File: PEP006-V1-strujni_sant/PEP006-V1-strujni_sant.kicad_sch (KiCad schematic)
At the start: 15 parts, among them J1 Screw_Terminal_01x02, J2 Conn_01x02_Pin, J3 Conn_01x02_Pin, J4 Conn_01x02_Pin

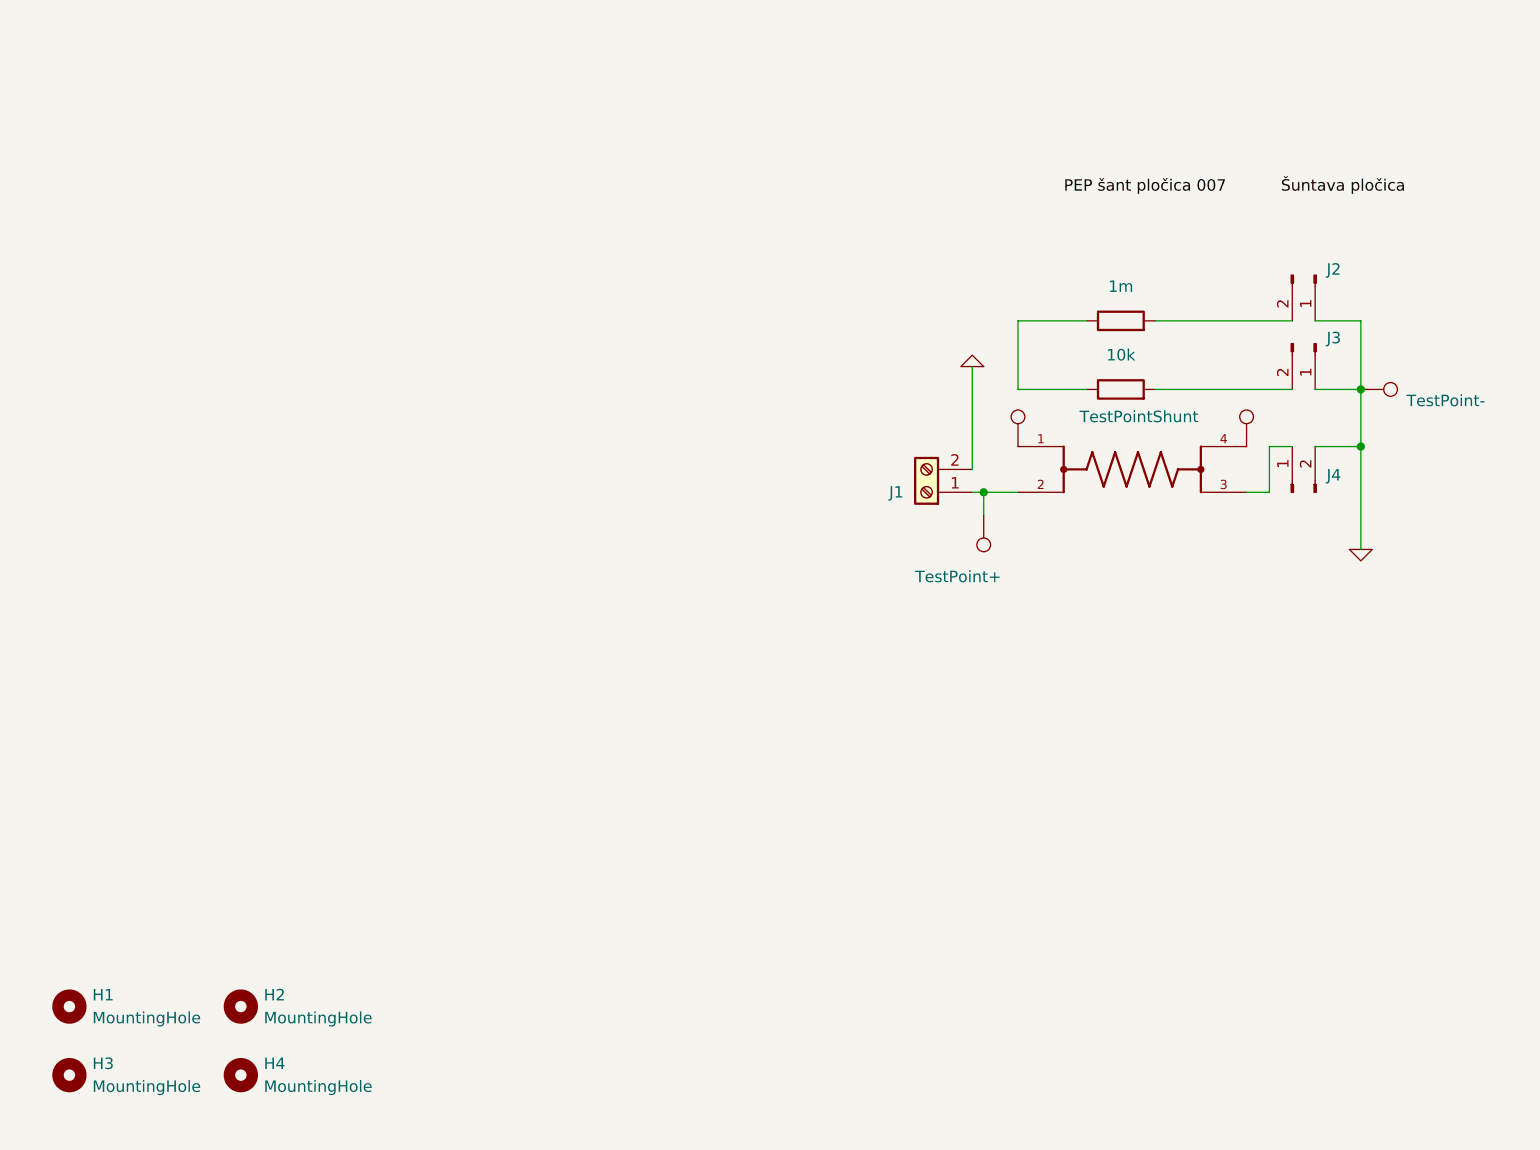
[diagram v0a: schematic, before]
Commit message: PEP006 and PEP009 update.
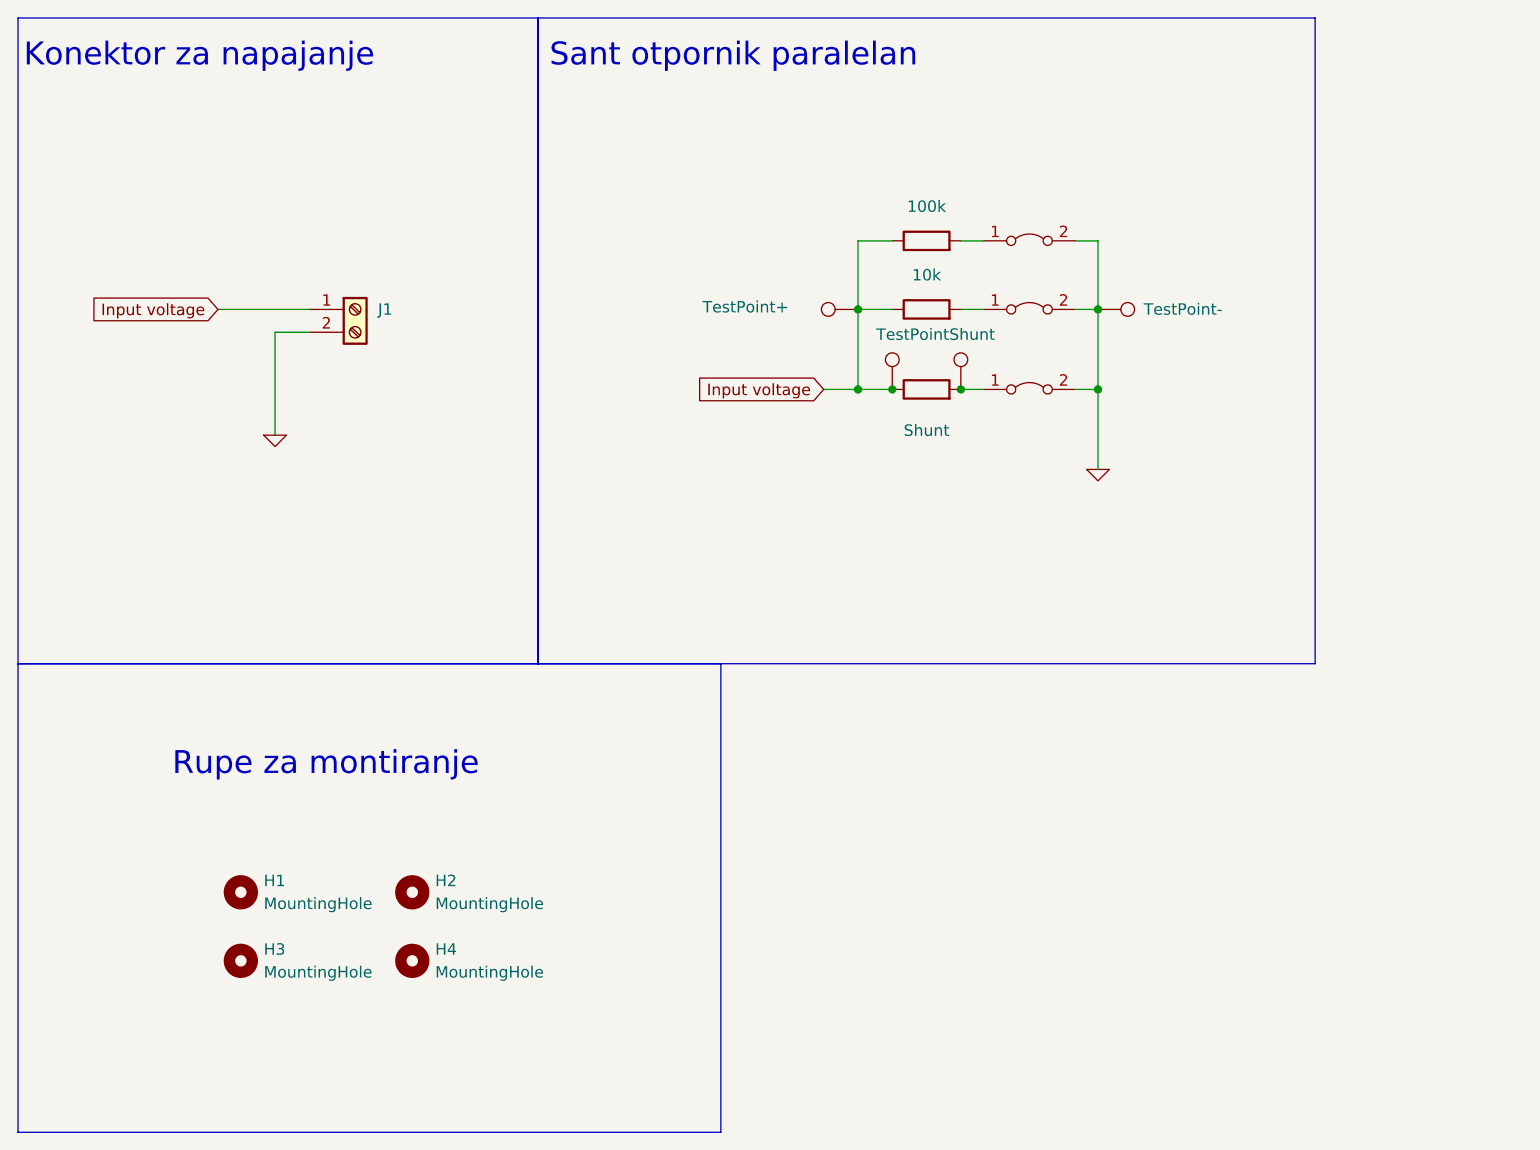
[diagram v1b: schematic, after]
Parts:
- removed J2, J3, J4: Conn_01x02_Pin, Connector_PinHeader_1.00mm:PinHeader_1x02_P1.00mm_Vertical, symbol Connector:Conn_01x02_Pin
- removed R1: 1m, Resistor_SMD:R_1206_3216Metric_Pad1.30x1.75mm_HandSolder, symbol Device:R
- removed R2: 10k, Resistor_SMD:R_1206_3216Metric_Pad1.30x1.75mm_HandSolder, symbol Device:R
- removed R7: WSK12161, 45x45_template-master:RES_WSK12161L000FEA, symbol WSK12161L000FEA:WSK12161L000FEA
- removed TP1: TestPoint-, TestPoint:TestPoint_Pad_D1.5mm, symbol Connector:TestPoint
- removed TP2, TP5: TestPointShunt, TestPoint:TestPoint_Pad_D1.5mm, symbol Connector:TestPoint
- removed TP4: TestPoint+, TestPoint:TestPoint_Pad_D1.5mm, symbol Connector:TestPoint
- added JP1, JP2, JP3: Jumper, Connector_PinHeader_2.54mm:PinHeader_1x02_P2.54mm_Vertical, symbol Jumper:Jumper_2_Bridged
- added R3: 100k, Resistor_SMD:R_1206_3216Metric_Pad1.30x1.75mm_HandSolder, symbol Device:R
- added R4: 10k, Resistor_SMD:R_1206_3216Metric_Pad1.30x1.75mm_HandSolder, symbol Device:R
- added R5: Shunt, WSK12161L000FEA (1):RES_WSK12161L000FEA, symbol Device:R
- added TP3: TestPoint+, TestPoint:TestPoint_Pad_D1.5mm, symbol Connector:TestPoint
- added TP6, TP7: TestPointShunt, TestPoint:TestPoint_Pad_D1.5mm, symbol Connector:TestPoint
- added TP8: TestPoint-, TestPoint:TestPoint_Pad_D1.5mm, symbol Connector:TestPoint
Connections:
- net 0: now also JP1.2 (B), JP2.2 (B), JP3.2 (B), TP8.1
- net Input voltage: now reaches J1.1 (Pin_1)
- net Input voltage: now also R3.1, R4.1, R5.1, TP3.1, TP6.1
- new net: JP3.1 (A), R5.2, TP7.1
- new net: JP1.1 (A), R3.2
- new net: JP2.1 (A), R4.2
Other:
- note added: "Konektor za napajanje"
- note added: "Rupe za montiranje"
- note added: "Sant otpornik paralelan"
- title: (none) -> Stujni šant
- moved on the sheet: H1, H2, H3, H4, J1

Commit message: PEP006 update.
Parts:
- removed R5: Shunt, WSK12161L000FEA (1):RES_WSK12161L000FEA, symbol Device:R
- added R1: Shunt, WSK12161L000FEA (1):RES_WSK12161L000FEA, symbol WSK12161L000FEA:WSK12161L000FEA
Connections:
- net Input voltage: now also R1.2; no longer TP6.1
- net at TP7.1: now also R1.1; no longer JP3.1 (A)
- new net: JP3.1 (A), R1.3
- new net: R1.4, TP6.1

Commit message: PEP006
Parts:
- R1: value Shunt -> 2m
- R3: value 100k -> 100
- R4: value 10k -> 1
- TP3, TP6, TP7, TP8: footprint TestPoint:TestPoint_Pad_D1.5mm -> Connector_PinHeader_2.54mm:PinHeader_1x01_P2.54mm_Vertical
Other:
- note added: "Shunt otpornici"
- note removed: "Sant otpornik paralelan"
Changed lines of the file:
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@@
-	)
-	(junction
-		(at 128.27 53.34)
-		(diameter 0)
-		(color 0 0 0 0)
 	)
 	(junction
@@
 	)
 	(junction
-		(at 125.73 58.42)
-		(diameter 0)
-		(color 0 0 0 0)
-	)
-	(junction
 		(at 140.97 53.34)
 		(diameter 0)
@@
 	(wire
 		(pts
-			(xy 123.19 58.42) (xy 125.73 58.42)
-		)
-		(stroke
-			(width 0)
-			(type default)
-		)
-	)
-	(wire
-		(pts
 			(xy 138.43 53.34) (xy 140.97 53.34)
 		)
@@
 		(pts
 			(xy 40.64 46.99) (xy 40.64 58.42)
-		)
-		(stroke
-			(width 0)
-			(type default)
-		)
-	)
-	(wire
-		(pts
-			(xy 132.08 53.34) (xy 128.27 53.34)
 		)
 		(stroke
@@
 		)
 	)
-	(text "Sant otpornik paralelan"
+	(text "Shunt otpornici"
 		(exclude_from_sim no)
 		(at 71.12 17.78 0)
@@
 			)
 		)
-		(property "Value" "Shunt"
+		(property "Value" "2m"
 			(at 115.57 53.086 0)
 			(effects
@@
 			)
 		)
-		(property "Footprint" "TestPoint:TestPoint_Pad_D1.5mm"
+		(property "Footprint" "Connector_PinHeader_2.54mm:PinHeader_1x01_P2.54mm_Vertical"
 			(at 120.65 58.42 0)
 			(effects
@@
 			)
 		)
-		(property "Value" "100k"
+		(property "Value" "100"
 			(at 115.57 33.02 90)
 			(effects
@@
 			)
 		)
-		(property "Value" "10k"
+		(property "Value" "1"
 			(at 115.57 40.64 90)
 			(effects
@@
 			)
 		)
-		(property "Footprint" "TestPoint:TestPoint_Pad_D1.5mm"
+		(property "Footprint" "Connector_PinHeader_2.54mm:PinHeader_1x01_P2.54mm_Vertical"
 			(at 100.33 58.42 0)
 			(effects
@@
 		)
 		(property "Value" "TestPoint-"
-			(at 146.05 44.45 90)
+			(at 141.986 41.656 90)
 			(effects
 				(font
@@
 			)
 		)
-		(property "Footprint" "TestPoint:TestPoint_Pad_D1.5mm"
+		(property "Footprint" "Connector_PinHeader_2.54mm:PinHeader_1x01_P2.54mm_Vertical"
 			(at 140.97 49.53 0)
 			(effects
@@
 		)
 		(property "Value" "TestPoint+"
-			(at 88.138 44.196 90)
+			(at 90.17 44.45 90)
 			(effects
 				(font
@@
 			)
 		)
-		(property "Footprint" "TestPoint:TestPoint_Pad_D1.5mm"
+		(property "Footprint" "Connector_PinHeader_2.54mm:PinHeader_1x01_P2.54mm_Vertical"
 			(at 105.41 39.37 0)
 			(effects

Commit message: PEP006 final commit, ready for production.
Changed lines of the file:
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@@
 	(text "Rupe za montiranje\n"
 		(exclude_from_sim no)
-		(at 29.21 96.52 0)
+		(at 12.7 88.9 0)
 		(effects
 			(font
